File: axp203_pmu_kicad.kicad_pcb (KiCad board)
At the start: 2 copper layers, 0 parts

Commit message: Updated PCB
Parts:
- added U1: AXP203, X_Powers:AXP203_QFN48, F.Cu at (147.1, 98.6)

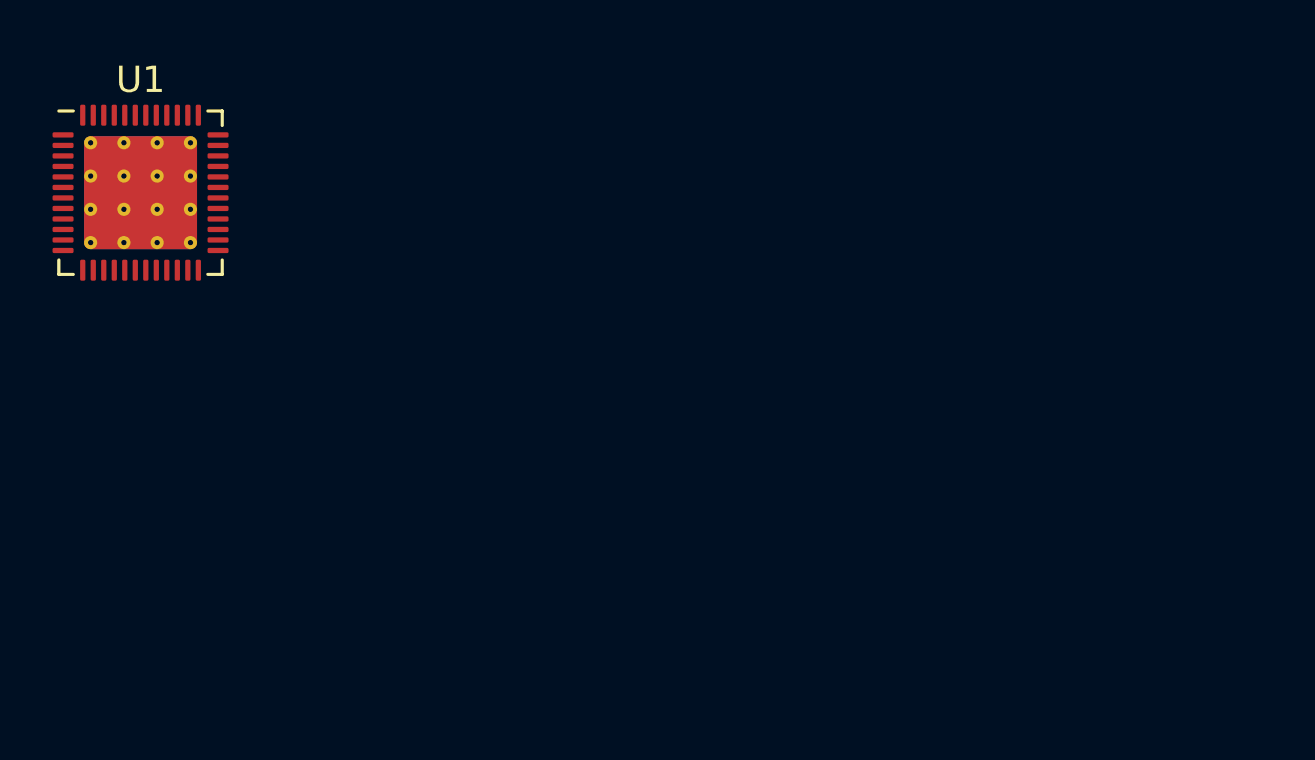
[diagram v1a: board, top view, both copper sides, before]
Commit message: Schematic finished, pcb components added in pcb, axp schematic checked
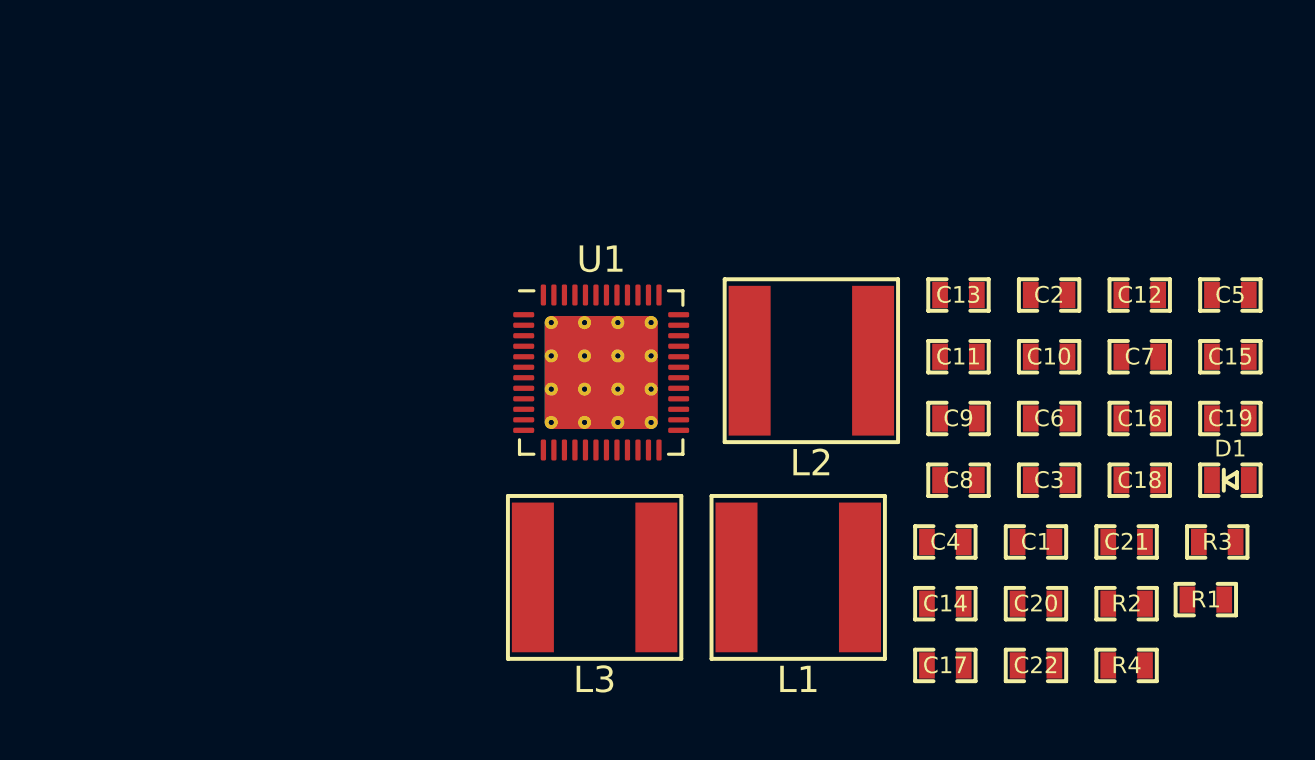
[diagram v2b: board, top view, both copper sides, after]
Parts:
- added C1: 10uF/10V, Capacitors_Smd_0603:10uF_10V_0603, F.Cu at (181.2, 111.9)
- added C10: 4.7uF/10V, Capacitors_Smd_0603:4_7uF_0603, F.Cu at (181.7, 104.9)
- added C11: 4.7uF/10V, Capacitors_Smd_0603:4_7uF_0603, F.Cu at (178.3, 104.9)
- added C12: 4.7uF/10V, Capacitors_Smd_0603:4_7uF_0603, F.Cu at (185.2, 102.5)
- added C13: 10uF/10V, Capacitors_Smd_0603:10uF_10V_0603, F.Cu at (178.3, 102.5)
- added C14: 10uF/10V, Capacitors_Smd_0603:10uF_10V_0603, F.Cu at (177.8, 114.3)
- added C15: 10uF/10V, Capacitors_Smd_0603:10uF_10V_0603, F.Cu at (188.6, 104.9)
- added C16: 10uF/10V, Capacitors_Smd_0603:10uF_10V_0603, F.Cu at (185.2, 107.2)
- added C17: 10uF/10V, Capacitors_Smd_0603:10uF_10V_0603, F.Cu at (177.8, 116.6)
- added C18: 10uF/10V, Capacitors_Smd_0603:10uF_10V_0603, F.Cu at (185.2, 109.6)
- added C19: 10uF/10V, Capacitors_Smd_0603:10uF_10V_0603, F.Cu at (188.6, 107.2)
- added C2: 10uF/10V, Capacitors_Smd_0603:10uF_10V_0603, F.Cu at (181.7, 102.5)
- added C20: 10uF/10V, Capacitors_Smd_0603:10uF_10V_0603, F.Cu at (181.2, 114.3)
- added C21: 100nF/50V, Capacitors_Smd_0603:100nF_0603, F.Cu at (184.7, 111.9)
- added C22: 10uF/10V, Capacitors_Smd_0603:10uF_10V_0603, F.Cu at (181.2, 116.6)
- added C3: 1uF/10V, Capacitors_Smd_0603:1uF_0603, F.Cu at (181.7, 109.6)
- added C4: 10uF/10V, Capacitors_Smd_0603:10uF_10V_0603, F.Cu at (177.8, 111.9)
- added C5: 10uF/10V, Capacitors_Smd_0603:10uF_10V_0603, F.Cu at (188.6, 102.5)
- added C6: 10uF/10V, Capacitors_Smd_0603:10uF_10V_0603, F.Cu at (181.7, 107.2)
- added C7: 10uF/10V, Capacitors_Smd_0603:10uF_10V_0603, F.Cu at (185.2, 104.9)
- added C8: 10uF/10V, Capacitors_Smd_0603:10uF_10V_0603, F.Cu at (178.3, 109.6)
- added C9: 4.7uF/10V, Capacitors_Smd_0603:4_7uF_0603, F.Cu at (178.3, 107.2)
- added D1: Green, Diodes:LED_KPT-1608CGCK, F.Cu at (188.6, 109.6)
- added L1: 4.7uH, Inductors:IHLP2020BZER4R7M01, F.Cu at (172.2, 113.3)
- added L2: 4.7uH, Inductors:IHLP2020BZER4R7M01, F.Cu at (172.7, 105.0)
- added L3: 4.7uH, Inductors:IHLP2020BZER4R7M01, F.Cu at (164.4, 113.3)
- added R1: 0.033R, Resistor_Smd_0603:0R033_0603, F.Cu at (187.7, 114.1)
- added R2: 100R/63mW, Resistor_Smd_0603:100R_0603, F.Cu at (184.7, 114.3)
- added R3: 1k, Resistor_Smd_0603:1k_0603, F.Cu at (188.1, 111.9)
- added R4: 1k, Resistor_Smd_0603:1k_0603, F.Cu at (184.7, 116.6)
- moved U1 18.8 mm to (164.7, 105.5)
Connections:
- U1 pad 10: (no net) -> /AXP203 PMU/DCDC2_VOUT
- U1 pad 11: (no net) -> /AXP203 PMU/LDO4_VOUT
- U1 pad 12: (no net) -> /AXP203 PMU/LDO2_VOUT
- U1 pad 13: (no net) -> /AXP203 PMU/DCDC3_VOUT
- U1 pad 14: (no net) -> /AXP203 PMU/IPS_VOUT
- U1 pad 15: (no net) -> Net-(L2-Pad1)
- U1 pad 16: (no net) -> GND
- U1 pad 17: (no net) -> /AXP203 PMU/DCDC3_VOUT
- U1 pad 21: (no net) -> /AXP203 PMU/IPS_VOUT
- U1 pad 22: (no net) -> GND
- U1 pad 23: (no net) -> Net-(R3-Pad1)
- U1 pad 24: (no net) -> Net-(C6-Pad1)
- U1 pad 26: (no net) -> Net-(C2-Pad1)
- U1 pad 28: (no net) -> /AXP203 PMU/LDO1_VOUT
- U1 pad 29: (no net) -> /AXP203 PMU/IPS_VOUT
- U1 pad 31: (no net) -> /AXP203 PMU/VBUS
- U1 pad 32: (no net) -> /AXP203 PMU/DCIN
- U1 pad 33: (no net) -> /AXP203 PMU/DCIN
- U1 pad 34: (no net) -> /AXP203 PMU/IPS_VOUT
- U1 pad 35: (no net) -> /AXP203 PMU/IPS_VOUT
- U1 pad 36: (no net) -> Net-(D1-Pad2)
- U1 pad 37: (no net) -> Net-(R2-Pad1)
- U1 pad 38: (no net) -> /AXP203 PMU/VBAT
- U1 pad 39: (no net) -> /AXP203 PMU/VBAT
- U1 pad 40: (no net) -> /AXP203 PMU/DCDC3_VOUT
- U1 pad 41: (no net) -> /AXP203 PMU/LDO3_VOUT
- U1 pad 42: (no net) -> /AXP203 PMU/VBAT
- U1 pad 43: (no net) -> /AXP203 PMU/VBAT
- U1 pad 44: (no net) -> /AXP203 PMU/IPS_VOUT
- U1 pad 45: (no net) -> Net-(L1-Pad2)
- U1 pad 46: (no net) -> GND
- U1 pad 49: Net-(U1-Pad49) -> GND
- U1 pad 7: (no net) -> /AXP203 PMU/IPS_VOUT
- U1 pad 8: (no net) -> Net-(L3-Pad1)
- U1 pad 9: (no net) -> GND
